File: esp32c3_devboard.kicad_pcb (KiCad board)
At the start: 2 copper layers, 40.6 x 25.4 mm, 56 parts, among them J1 Conn_01x15_Male, J2 Conn_01x15_Male, J4 USB_C_Receptacle_USB2.0, Q1 S8050, Q2 S8050, SW1 BOOT, SW2 RST, U1 USB2514B_Bi, U2 CH340X, U3 ESP32-C3-WROOM-02, U4 AMS1117-3.3, U5 SRV05-4, Y1 24MHz

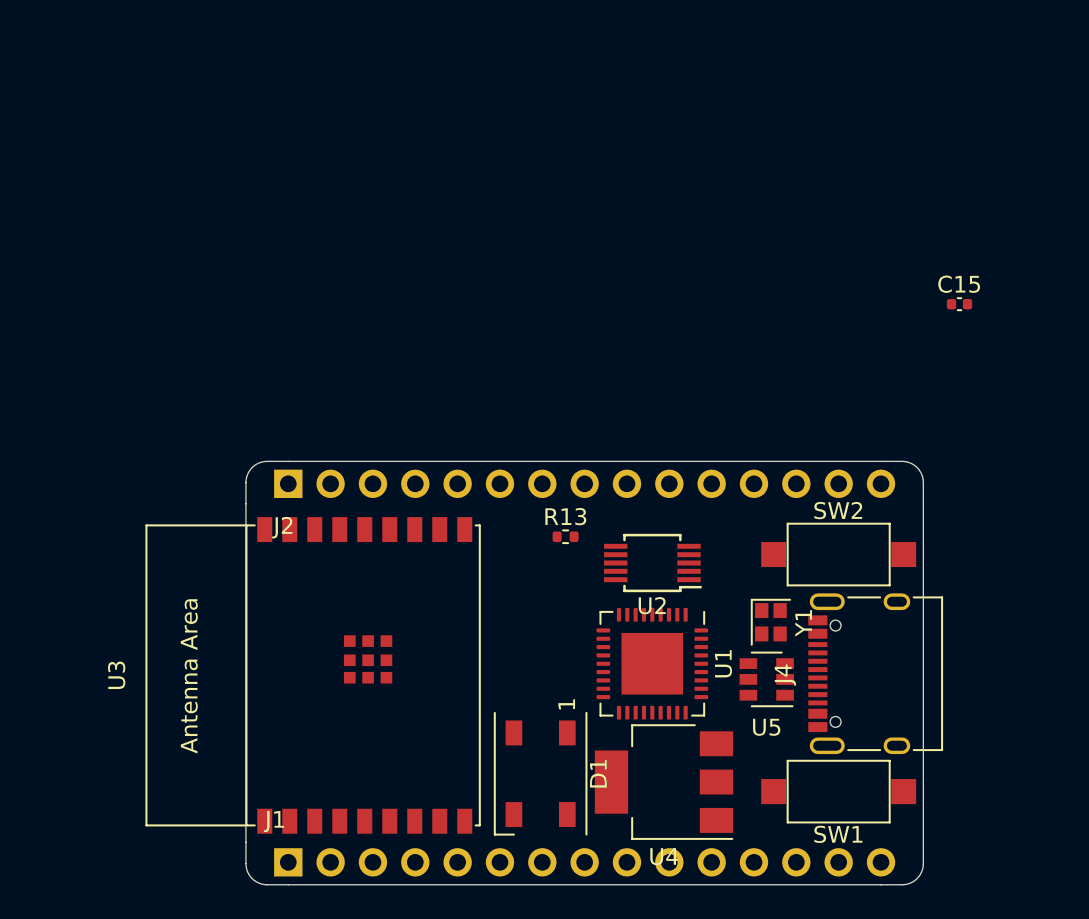
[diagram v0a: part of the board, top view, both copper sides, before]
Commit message: Change USB UART adapter to CP2102
Signed-off-by: Tomislav Milkovic <tomislav.milkovic95@gmail.com>
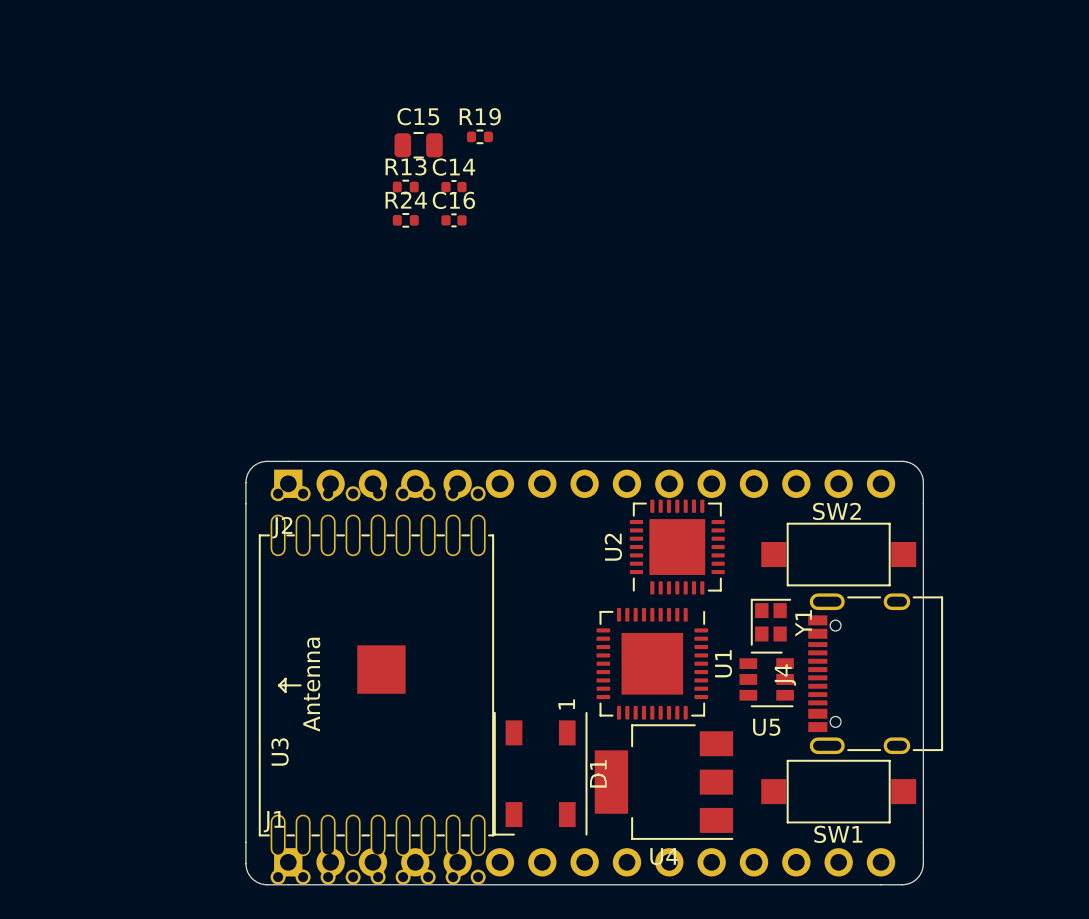
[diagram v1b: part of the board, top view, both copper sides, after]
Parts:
- added C14: 100n, Capacitor_SMD:C_0402_1005Metric, F.Cu at (121.7, 95.3)
- added C16: 1uF, Capacitor_SMD:C_0402_1005Metric, F.Cu at (121.7, 97.3)
- added R19: 24K, Resistor_SMD:R_0402_1005Metric, F.Cu at (123.3, 92.3)
- added R24: 47K, Resistor_SMD:R_0402_1005Metric, F.Cu at (118.8, 97.3)
- C15: value 100n -> 10u; footprint Capacitor_SMD:C_0402_1005Metric -> Capacitor_SMD:C_0805_2012Metric
- R13: value 4K7 -> 1K
- U2: value CH340X -> CP2102N-A01-GQFN28; footprint Package_SO:MSOP-10_3x3mm_P0.5mm -> Package_DFN_QFN:QFN-28-1EP_5x5mm_P0.5mm_EP3.35x3.35mm
- U3: footprint Espressif:ESP32-C3-WROOM-02 -> Espressif custom:ESP32-C3-WROOM-02-SOCKET
- moved C15 33.8 mm to (119.6, 92.8)
- moved R13 23.1 mm to (118.8, 95.3)
- moved U2 1.78 mm to (135.1, 116.9), turned to 90 degrees
- moved U3 1.00 mm to (115.3, 125.2)
- turned SW2 to 180 degrees
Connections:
- R13 pad 1: GND -> +3V3
- R13 pad 2: /ESP32-C3 module/ESP32_UART_DTR -> /USB-UART bridge/RSTb
- U2 pad 1: /USB hub/DOWNSTREAM_USB1_D+ -> (no net)
- U2 pad 10: +3V3 -> (no net)
- U2 pad 2: /USB hub/DOWNSTREAM_USB1_D- -> (no net)
- U2 pad 4: /ESP32-C3 module/ESP32_UART_RTS -> /USB hub/DOWNSTREAM_USB1_D+
- U2 pad 5: (no net) -> /USB hub/DOWNSTREAM_USB1_D-
- U2 pad 6: /ESP32-C3 module/ESP32_UART_DTR -> +3V3
- U2 pad 8: /ESP32-C3 module/ESP32_UART_RXD -> /USB-UART bridge/VBUS
- U2 pad 9: /ESP32-C3 module/ESP32_UART_TXD -> /USB-UART bridge/RSTb
- U5 pad 1: /USB connector and power supply/USB_D- -> /USB connector and power supply/CONN_USB_D-
- U5 pad 3: /USB connector and power supply/USB_D+ -> /USB connector and power supply/CONN_USB_D+
- U5 pad 4: /USB connector and power supply/USB_D+ -> /USB connector and power supply/CONN_USB_D+
- U5 pad 6: /USB connector and power supply/USB_D- -> /USB connector and power supply/CONN_USB_D-
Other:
- copper layers 2 -> 4

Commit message: Add LCSC part numbers for all components
Signed-off-by: Tomislav Milkovic <tomislav.milkovic95@gmail.com>
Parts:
- removed C3: 1u, Capacitor_SMD:C_0402_1005Metric
- removed R23: 10M, Resistor_SMD:R_0402_1005Metric
- C11: value 1u -> 10u
- C12, C13: value 18p -> 6p8
- C15, C20, C21: footprint Capacitor_SMD:C_0805_2012Metric -> Capacitor_SMD:C_0603_1608Metric
- D1: footprint LED_SMD:LED_WS2812B_PLCC4_5.0x5.0mm_P3.2mm -> LED_custom:LED_WS2812B_2.0x2.0mm_P1.13mm
- R11, R9: value 10K -> 100K
- R20: footprint Resistor_SMD:R_0603_1608Metric -> Resistor_SMD:R_0402_1005Metric
- moved D1 11.6 mm to (138.4, 129.4), turned to 90 degrees
- moved U4 1.80 mm to (132.5, 131.0)

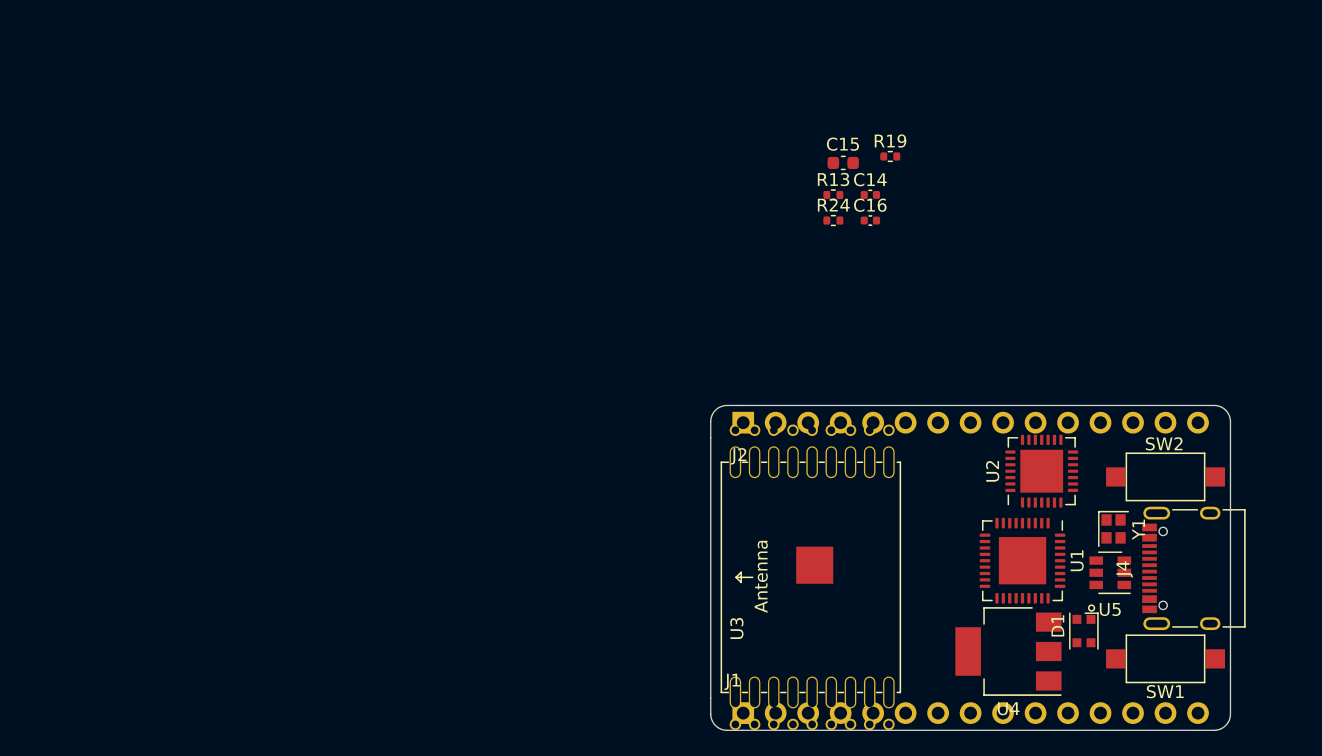
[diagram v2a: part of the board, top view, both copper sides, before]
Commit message: Replace WS2812B with SK6805 RGB LED
Signed-off-by: Tomislav Milkovic <tomislav.milkovic95@gmail.com>
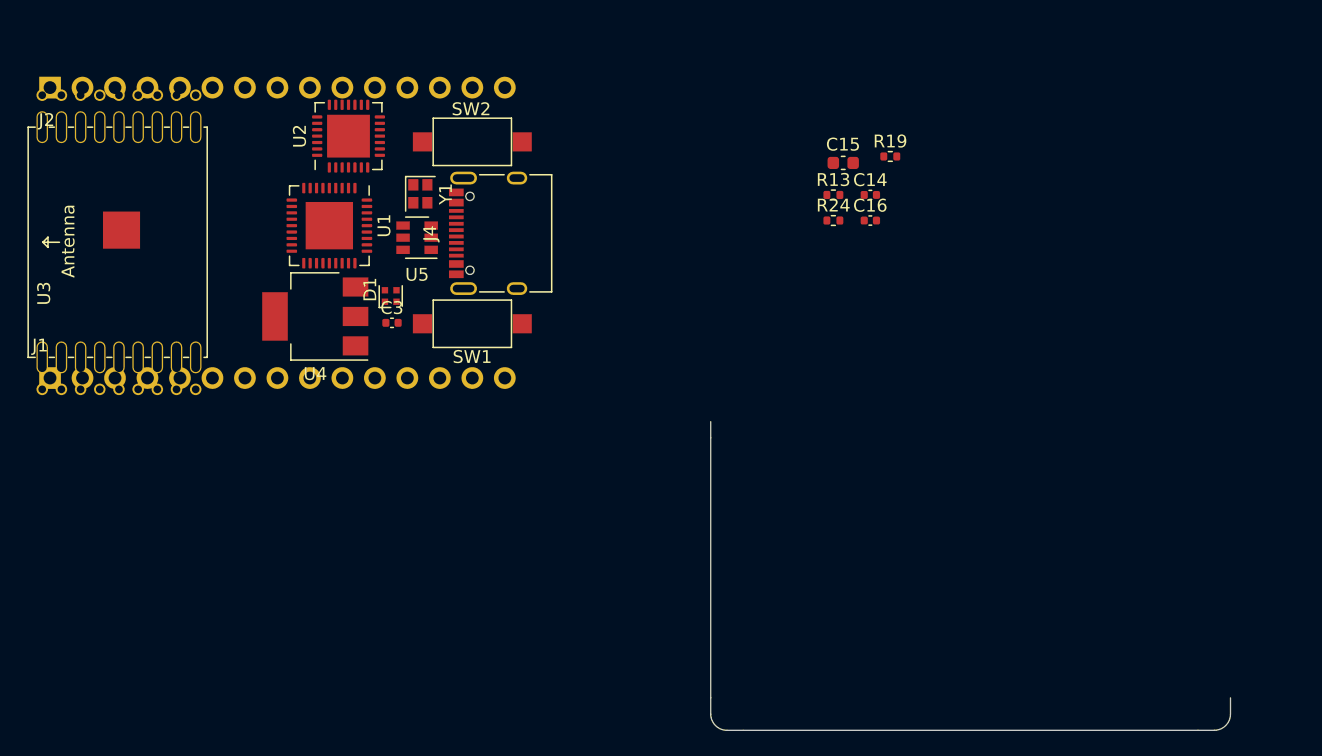
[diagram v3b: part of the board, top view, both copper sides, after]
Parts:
- added C3: 100n, Capacitor_SMD:C_0402_1005Metric, F.Cu at (84.3, 105.3)
- D1: value WS2812B -> SK6805-EC14; footprint LED_custom:LED_WS2812B_2.0x2.0mm_P1.13mm -> LED_custom:LED_SK6805_E14_1.4x1.4mm_P0.4mm
- moved D1 60.2 mm to (84.2, 103.2)
- moved J2 60.2 mm to (57.6, 86.9)
- moved SW1 60.2 mm to (90.6, 105.4)
- moved SW2 60.2 mm to (90.6, 91.1)
- moved U4 60.2 mm to (78.3, 104.8)
- moved Y1 60.2 mm to (86.5, 95.2)
- moved U3 60.2 mm to (61.1, 99.0)
- moved J1 60.2 mm to (57.6, 109.6)
- moved J4 60.2 mm to (93.0, 98.3)
- moved U1 60.2 mm to (79.4, 97.7)
- moved U2 60.2 mm to (80.9, 90.7)
- moved U5 60.2 mm to (86.3, 98.6)
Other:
- board size 40.6 x 25.4 mm -> 40.6 x 24.1 mm
- net class USB: clearance 0.2 -> 0.25; trace_width 0.25 -> 0.2934
- rule trace_min: 0.127 -> 0.1

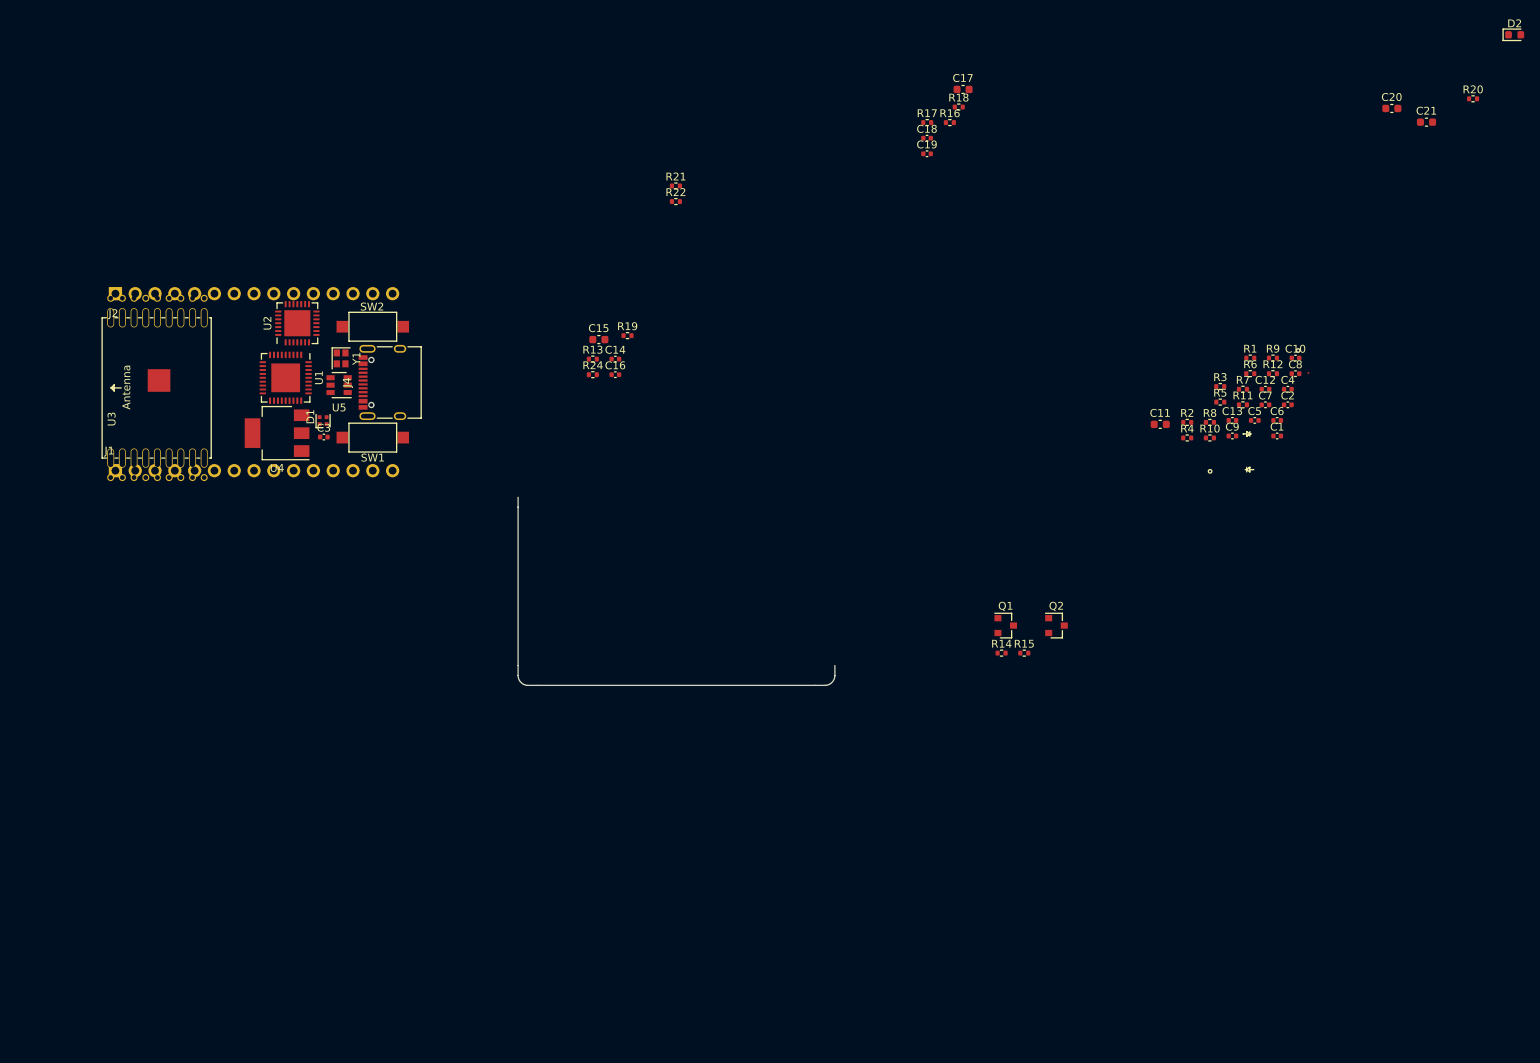
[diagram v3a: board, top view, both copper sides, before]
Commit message: PCB: Rough component placement done
Signed-off-by: Tomislav Milkovic <tomislav.milkovic95@gmail.com>
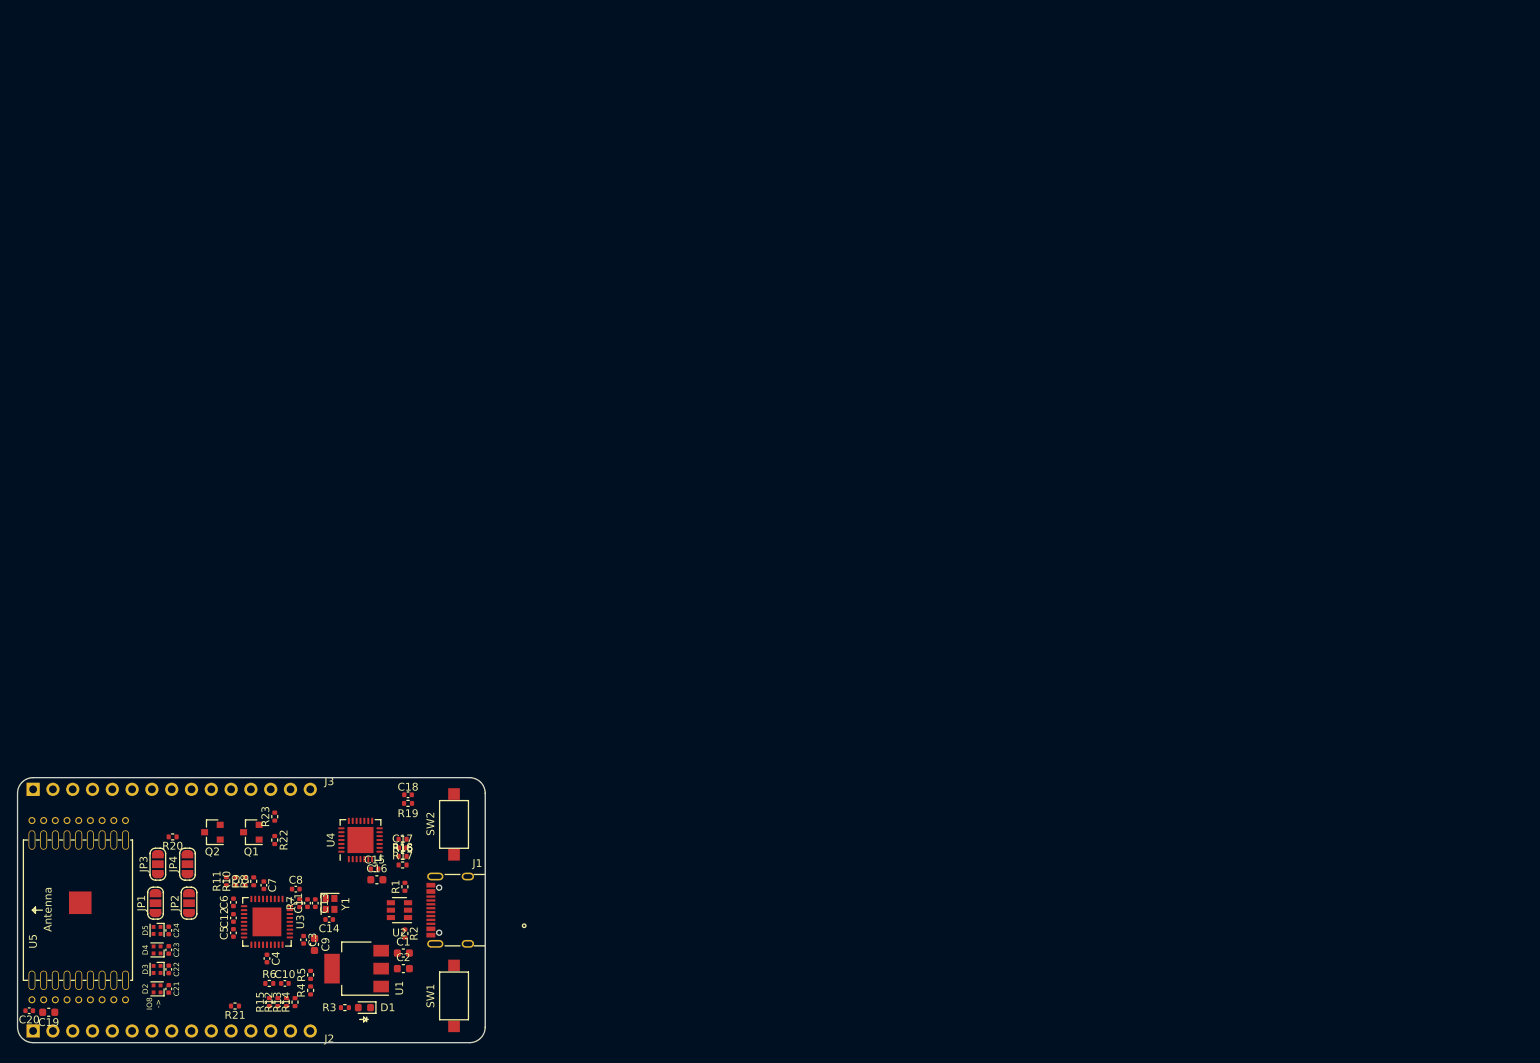
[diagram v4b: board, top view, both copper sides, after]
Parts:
- added C22: 100n, Capacitor_SMD:C_0402_1005Metric, F.Cu at (64.4, 173.6)
- added C23: 100n, Capacitor_SMD:C_0402_1005Metric, F.Cu at (64.4, 171.1)
- added C24: 100n, Capacitor_SMD:C_0402_1005Metric, F.Cu at (64.4, 168.6)
- added D3: SK6805, LED_custom:LED_SK6805_E14_1.4x1.4mm_P0.4mm, F.Cu at (62.9, 173.6)
- added D4: SK6805, LED_custom:LED_SK6805_E14_1.4x1.4mm_P0.4mm, F.Cu at (62.9, 171.1)
- added D5: SK6805, LED_custom:LED_SK6805_E14_1.4x1.4mm_P0.4mm, F.Cu at (62.9, 168.6)
- added JP1: GPIO18_SB, Jumper:SolderJumper-3_P1.3mm_Open_RoundedPad1.0x1.5mm, F.Cu at (62.7, 165.1)
- added JP2: GPIO19_SB, Jumper:SolderJumper-3_P1.3mm_Open_RoundedPad1.0x1.5mm, F.Cu at (67.0, 165.1)
- added JP3: GPIO20_SB, Jumper:SolderJumper-3_P1.3mm_Open_RoundedPad1.0x1.5mm, F.Cu at (63.0, 160.1)
- added JP4: GPIO21_SB, Jumper:SolderJumper-3_P1.3mm_Open_RoundedPad1.0x1.5mm, F.Cu at (66.8, 160.1)
- D2: renamed from D1; value SK6805-EC14 -> SK6805
- U5: renamed from U3; value ESP32-C3-WROOM-02 -> ESP32-C3-WROOM-02-SOCKET
- moved D1 193.3 mm to (89.5, 178.5), turned to 180 degrees
- moved R3 185.9 mm to (87.0, 178.5)
- moved C2 170.4 mm to (94.5, 173.5)
- moved C1 166.8 mm to (94.5, 171.5)
- moved C19 166.7 mm to (49.0, 179.1)
- moved C20 160.6 mm to (46.5, 178.9), turned to 180 degrees
- moved C6 152.2 mm to (72.7, 165.0), turned to 90 degrees
- moved C12 151.3 mm to (72.7, 167.0), turned to 90 degrees
- moved R13 151.2 mm to (79.5, 177.8), turned to 90 degrees
- moved R6 149.3 mm to (77.3, 175.4)
- moved R14 149.1 mm to (80.6, 177.8), turned to 90 degrees
- moved C5 148.7 mm to (72.7, 168.9), turned to 270 degrees
- moved C4 146.8 mm to (77.0, 172.2), turned to 270 degrees
- moved R15 146.5 mm to (77.3, 177.8), turned to 90 degrees
- moved R10 145.5 mm to (73.0, 162.3), turned to 90 degrees
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- renumbered C20 to C1, C1 to C10, C2 to C11, C4 to C12, C12 to C13, C13 to C14, C14 to C15, C15 to C16, C16 to C17, C19 to C18, C17 to C19, C21 to C2, C18 to C20, C3 to C21, C5 to C3, C6 to C4, C7 to C5, C8 to C6, C9 to C7, C10 to C8, C11 to C9, D2 to D1, J4 to J1, J1 to J2, J2 to J3, R21 to R1, R6 to R10, R8 to R11, R10 to R12, R9 to R13, R12 to R14, R11 to R15, R13 to R16, R19 to R17, R24 to R18, R18 to R19, R22 to R2, R16 to R20, R17 to R21, R14 to R22, R15 to R23, R20 to R3, R3 to R4, R4 to R5, R1 to R6, R2 to R7, R5 to R8, R7 to R9, U4 to U1, U5 to U2, U1 to U3, U2 to U4
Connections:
- D2 pad 2: (no net) -> Net-(D2-Pad2)
- J3 pad 10: /ESP32-C3 module/ESP32_UART_TXD -> /ESP32-C3 module/GPIO21_HEADER
- J3 pad 12: /USB hub/DOWNSTREAM_USB2_D- -> /ESP32-C3 module/GPIO18_HEADER
- J3 pad 13: /USB hub/DOWNSTREAM_USB2_D+ -> /ESP32-C3 module/GPIO19_HEADER
- J3 pad 9: /ESP32-C3 module/ESP32_UART_RXD -> /ESP32-C3 module/GPIO20_HEADER
- U5 pad 11: /ESP32-C3 module/ESP32_UART_RXD -> /ESP32-C3 module/GPIO20
- U5 pad 12: /ESP32-C3 module/ESP32_UART_TXD -> /ESP32-C3 module/GPIO21
- U5 pad 13: /USB hub/DOWNSTREAM_USB2_D- -> /ESP32-C3 module/GPIO18
- U5 pad 14: /USB hub/DOWNSTREAM_USB2_D+ -> /ESP32-C3 module/GPIO19
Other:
- board size 40.6 x 24.1 mm -> 60 x 34 mm
- board text added: "IO8 ->"
